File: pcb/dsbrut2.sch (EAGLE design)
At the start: 11 parts, among them IC1 4175D, IC2 74HC125D, IC3 MEGA8-AI

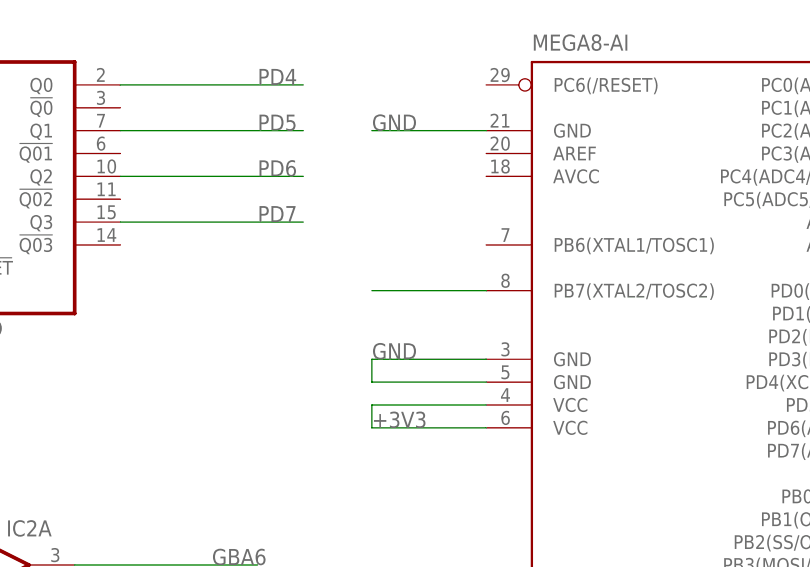
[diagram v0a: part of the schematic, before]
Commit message: updated isp progheader - please verify orientation
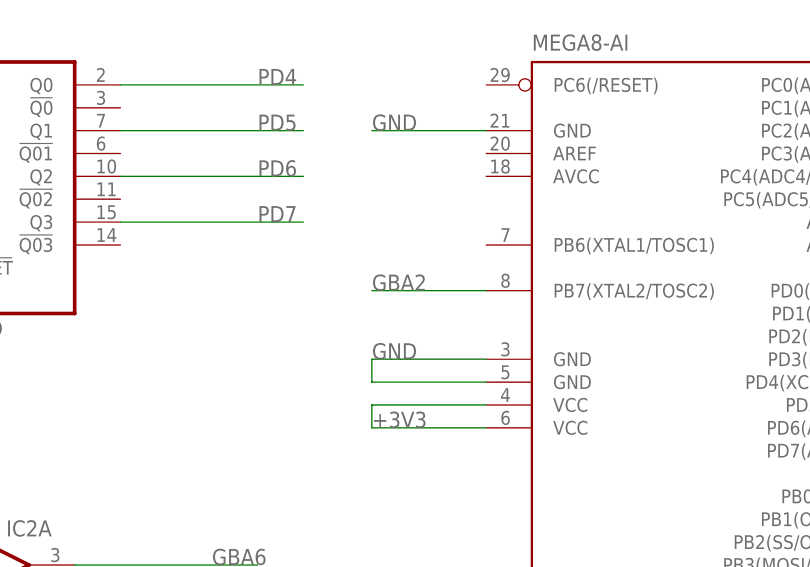
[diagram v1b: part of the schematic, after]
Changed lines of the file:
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@@
 <layer number="122" name="_bsilk" color="7" fill="1" visible="yes" active="yes"/>
 <layer number="125" name="_tNames" color="7" fill="1" visible="yes" active="yes"/>
+<layer number="131" name="prix" color="7" fill="1" visible="yes" active="yes"/>
+<layer number="132" name="test" color="7" fill="1" visible="yes" active="yes"/>
 <layer number="144" name="Drill_legend" color="7" fill="1" visible="yes" active="yes"/>
 <layer number="151" name="HeatSink" color="7" fill="1" visible="yes" active="yes"/>
@@
 <pinref part="IC3" gate="G$1" pin="PB7(XTAL2/TOSC2)"/>
 <wire x1="109.22" y1="127" x2="96.52" y2="127" width="0.1524" layer="91"/>
-</segment>
-<segment>
+<label x="96.52" y="127" size="1.778" layer="95"/>
+</segment>
+<segment>

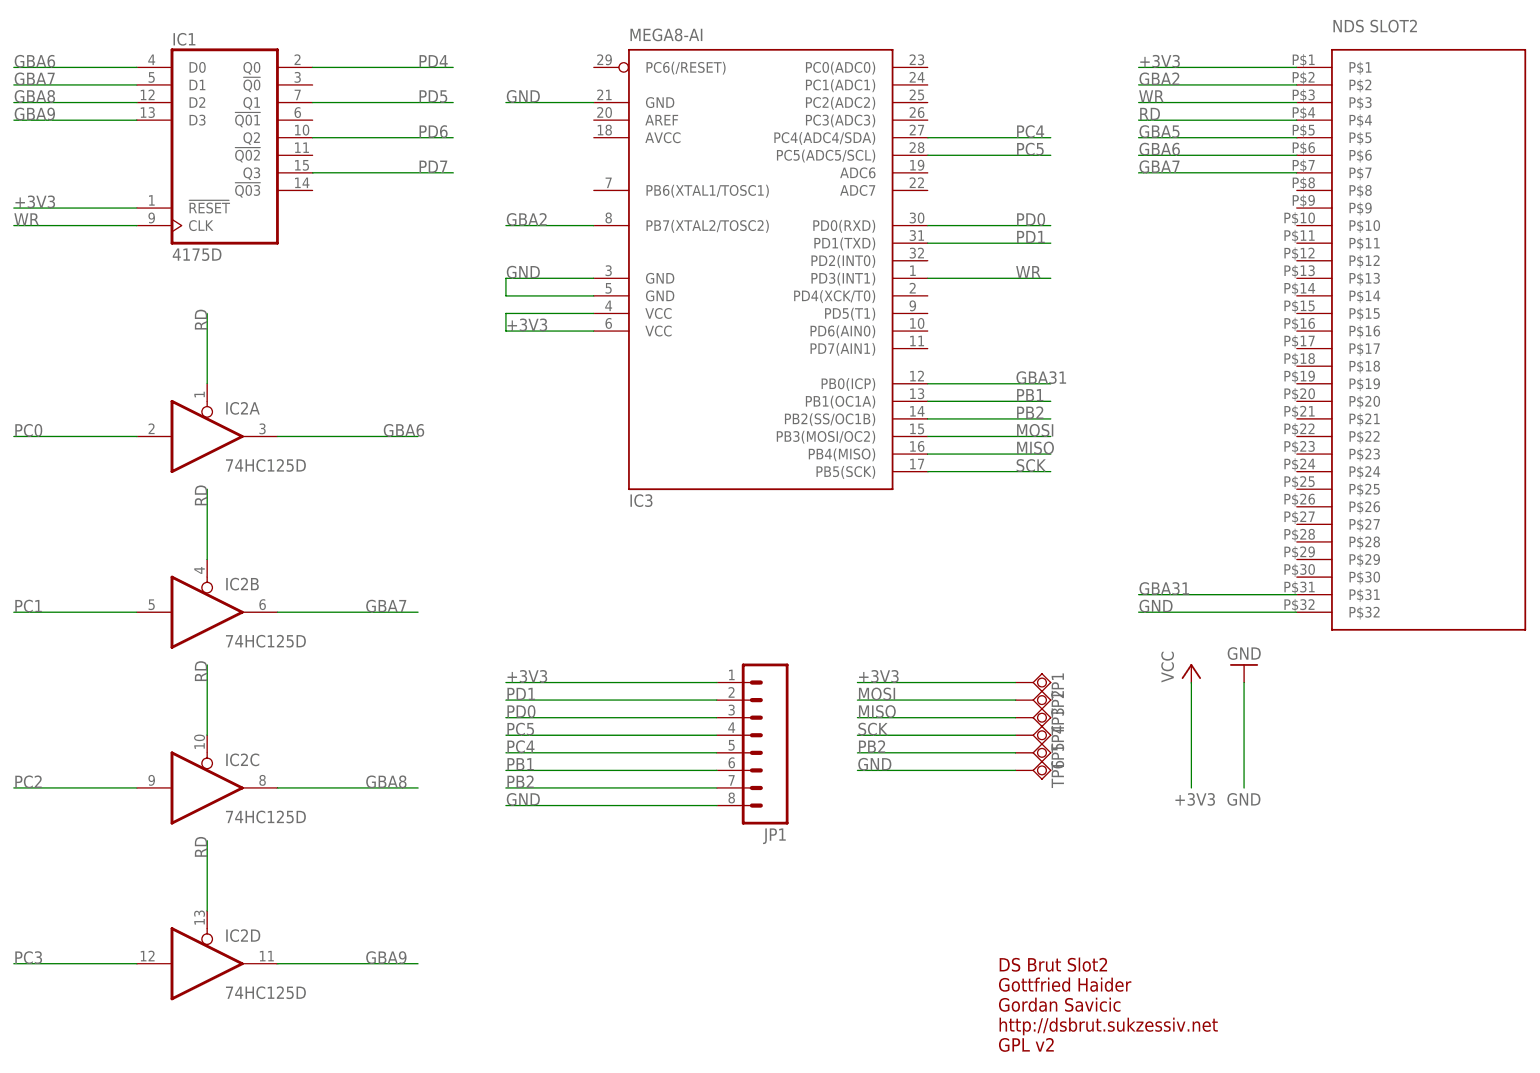
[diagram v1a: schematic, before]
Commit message: added rst, sck led, aref vcc, cleanup
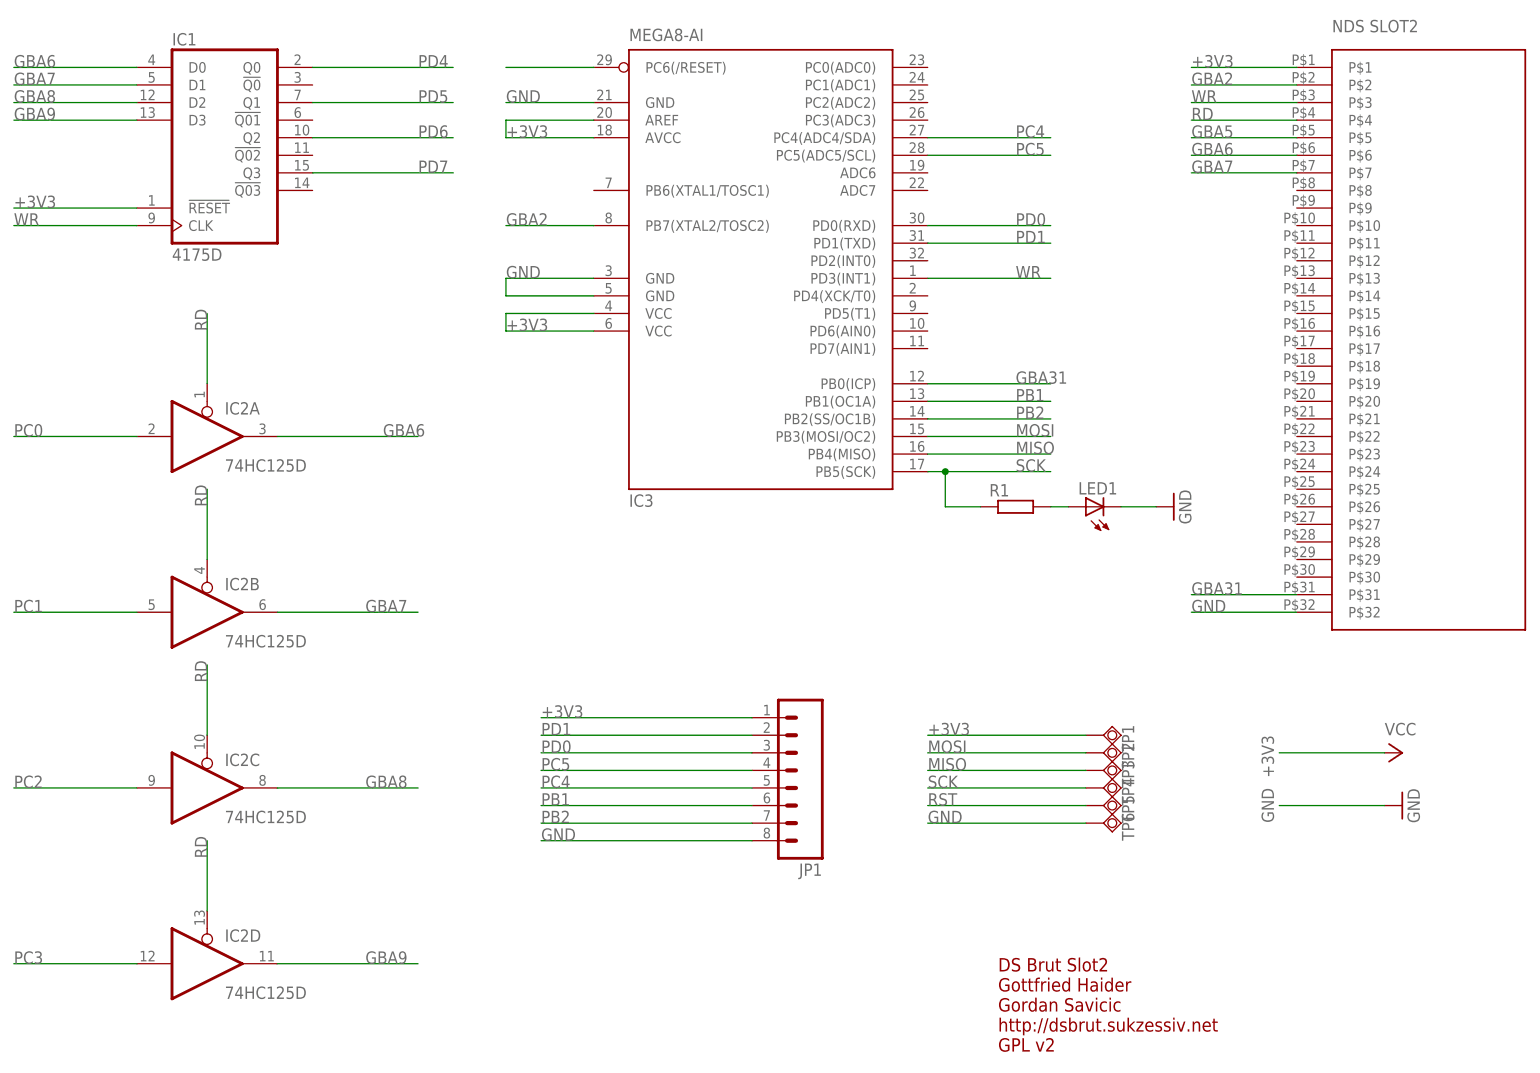
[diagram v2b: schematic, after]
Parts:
- added LED1: (no value), SparkFunEagle-6-6-07:LED0603
- added R1: (no value), rcl:R-EU_M0805
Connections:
- new net N$4: LED1.A, R1.2
- new net RST: IC3.PC6(/RESET), TP5.TP
- net +3V3: now also IC3.AREF, IC3.AVCC
- net GND: now also LED1.C
- net PB2: no longer TP5.TP
- net SCK: now also R1.1
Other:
- moved on the sheet: JP1, TP1, TP2, TP3, TP4, TP5, TP6

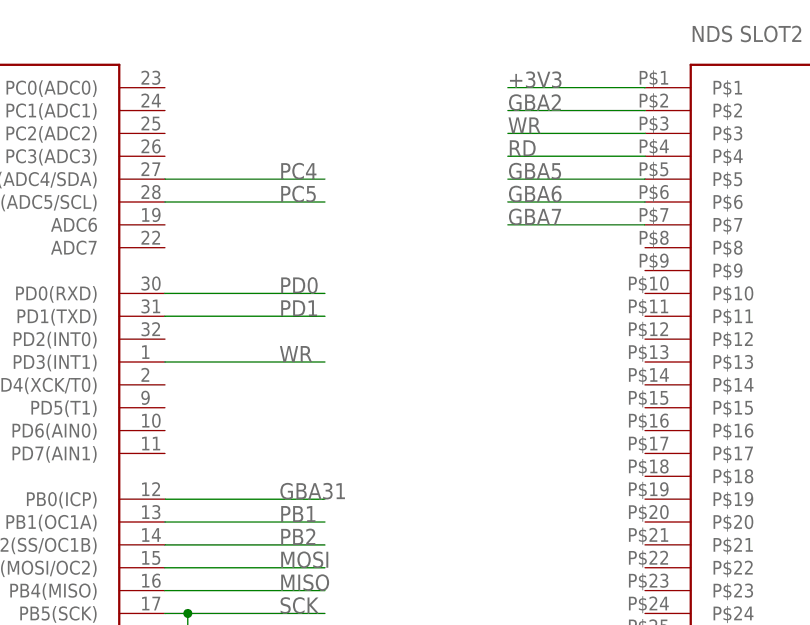
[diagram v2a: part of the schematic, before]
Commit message: Add GBA{8,9} and connections between IC{1,2} and the AtMega
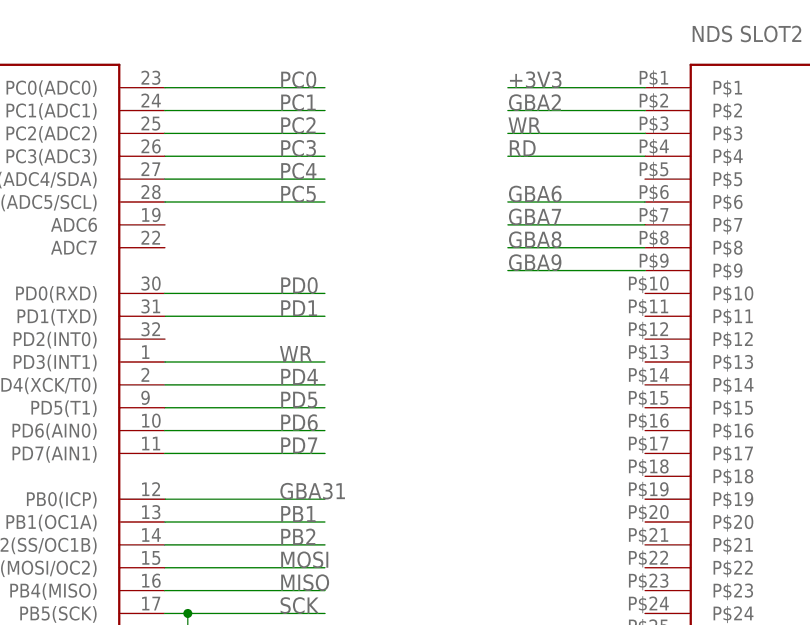
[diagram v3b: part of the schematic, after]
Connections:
- removed net GBA5: U$1.P$5
- net GBA8: now also U$1.P$8
- net GBA9: now also U$1.P$9
- net PC0: now also IC3.PC0(ADC0)
- net PC1: now also IC3.PC1(ADC1)
- net PC2: now also IC3.PC2(ADC2)
- net PC3: now also IC3.PC3(ADC3)
- net PD4: now also IC3.PD4(XCK/T0)
- net PD5: now also IC3.PD5(T1)
- net PD6: now also IC3.PD6(AIN0)
- net PD7: now also IC3.PD7(AIN1)
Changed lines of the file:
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@@
 <label x="83.82" y="149.86" size="1.778" layer="95"/>
+</segment>
+<segment>
+<pinref part="IC3" gate="G$1" pin="PD4(XCK/T0)"/>
+<wire x1="157.48" y1="116.84" x2="175.26" y2="116.84" width="0.1524" layer="91"/>
+<label x="170.18" y="116.84" size="1.778" layer="95"/>
 </segment>
 </net>
@@
 <label x="83.82" y="144.78" size="1.778" layer="95"/>
 </segment>
+<segment>
+<pinref part="IC3" gate="G$1" pin="PD5(T1)"/>
+<wire x1="157.48" y1="114.3" x2="175.26" y2="114.3" width="0.1524" layer="91"/>
+<label x="170.18" y="114.3" size="1.778" layer="95"/>
+</segment>
 </net>
 <net name="WR" class="0">
@@
 <label x="83.82" y="139.7" size="1.778" layer="95"/>
 </segment>
+<segment>
+<pinref part="IC3" gate="G$1" pin="PD6(AIN0)"/>
+<wire x1="157.48" y1="111.76" x2="175.26" y2="111.76" width="0.1524" layer="91"/>
+<label x="170.18" y="111.76" size="1.778" layer="95"/>
+</segment>
 </net>
 <net name="GBA8" class="0">
@@
 <label x="76.2" y="45.72" size="1.778" layer="95"/>
 </segment>
+<segment>
+<pinref part="U$1" gate="G$1" pin="P$8"/>
+<wire x1="210.82" y1="132.08" x2="195.58" y2="132.08" width="0.1524" layer="91"/>
+<label x="195.58" y="132.08" size="1.778" layer="95"/>
+</segment>
 </net>
 <net name="GBA9" class="0">
@@
 <label x="76.2" y="20.32" size="1.778" layer="95"/>
 </segment>
+<segment>
+<pinref part="U$1" gate="G$1" pin="P$9"/>
+<wire x1="210.82" y1="129.54" x2="195.58" y2="129.54" width="0.1524" layer="91"/>
+<label x="195.58" y="129.54" size="1.778" layer="95"/>
+</segment>
 </net>
 <net name="PD7" class="0">
@@
 <label x="83.82" y="134.62" size="1.778" layer="95"/>
 </segment>
+<segment>
+<pinref part="IC3" gate="G$1" pin="PD7(AIN1)"/>
+<wire x1="157.48" y1="109.22" x2="175.26" y2="109.22" width="0.1524" layer="91"/>
+<label x="170.18" y="109.22" size="1.778" layer="95"/>
+</segment>
 </net>
 <net name="PC3" class="0">
@@
 <label x="25.4" y="20.32" size="1.778" layer="95"/>
 </segment>
+<segment>
+<pinref part="IC3" gate="G$1" pin="PC3(ADC3)"/>
+<wire x1="157.48" y1="142.24" x2="175.26" y2="142.24" width="0.1524" layer="91"/>
+<label x="170.18" y="142.24" size="1.778" layer="95"/>
+</segment>
 </net>
 <net name="PC1" class="0">
@@
 <label x="25.4" y="71.12" size="1.778" layer="95"/>
 </segment>
+<segment>
+<pinref part="IC3" gate="G$1" pin="PC1(ADC1)"/>
+<wire x1="157.48" y1="147.32" x2="175.26" y2="147.32" width="0.1524" layer="91"/>
+<label x="170.18" y="147.32" size="1.778" layer="95"/>
+</segment>
 </net>
 <net name="PC0" class="0">
@@
 <label x="25.4" y="96.52" size="1.778" layer="95"/>
 </segment>
+<segment>
+<pinref part="IC3" gate="G$1" pin="PC0(ADC0)"/>
+<wire x1="157.48" y1="149.86" x2="175.26" y2="149.86" width="0.1524" layer="91"/>
+<label x="170.18" y="149.86" size="1.778" layer="95"/>
+</segment>
 </net>
 <net name="RD" class="0">
@@
 <label x="25.4" y="45.72" size="1.778" layer="95"/>
 </segment>
+<segment>
+<pinref part="IC3" gate="G$1" pin="PC2(ADC2)"/>
+<wire x1="157.48" y1="144.78" x2="175.26" y2="144.78" width="0.1524" layer="91"/>
+<label x="170.18" y="144.78" size="1.778" layer="95"/>
+</segment>
 </net>
 <net name="GBA31" class="0">
@@
 </segment>
 </net>
-<net name="GBA5" class="0">
-<segment>
-<pinref part="U$1" gate="G$1" pin="P$5"/>
-<wire x1="210.82" y1="139.7" x2="195.58" y2="139.7" width="0.1524" layer="91"/>
-<label x="195.58" y="139.7" size="1.778" layer="95"/>
-</segment>
-</net>

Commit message: Connected RD to ATmega, added TX/RX labels, removed ground plane underneath Slot -2 pins
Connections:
- net RD: now also IC3.PD2(INT0)
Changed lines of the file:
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@@
 <label x="195.58" y="142.24" size="1.778" layer="95"/>
+</segment>
+<segment>
+<pinref part="IC3" gate="G$1" pin="PD2(INT0)"/>
+<wire x1="157.48" y1="121.92" x2="175.26" y2="121.92" width="0.1524" layer="91"/>
+<label x="170.18" y="121.92" size="1.778" layer="95"/>
 </segment>
 </net>

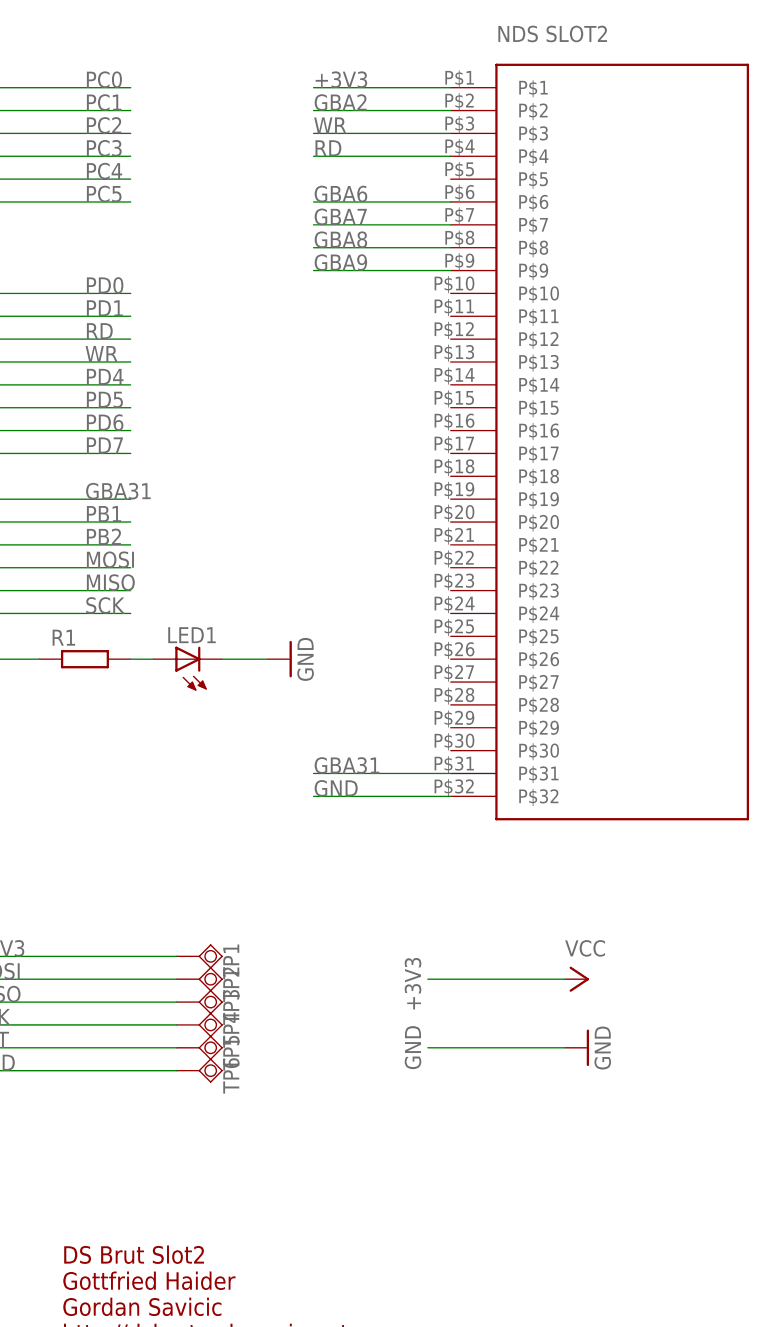
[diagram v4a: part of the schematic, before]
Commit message: added fuse, fixed ic1 power supply with VSS
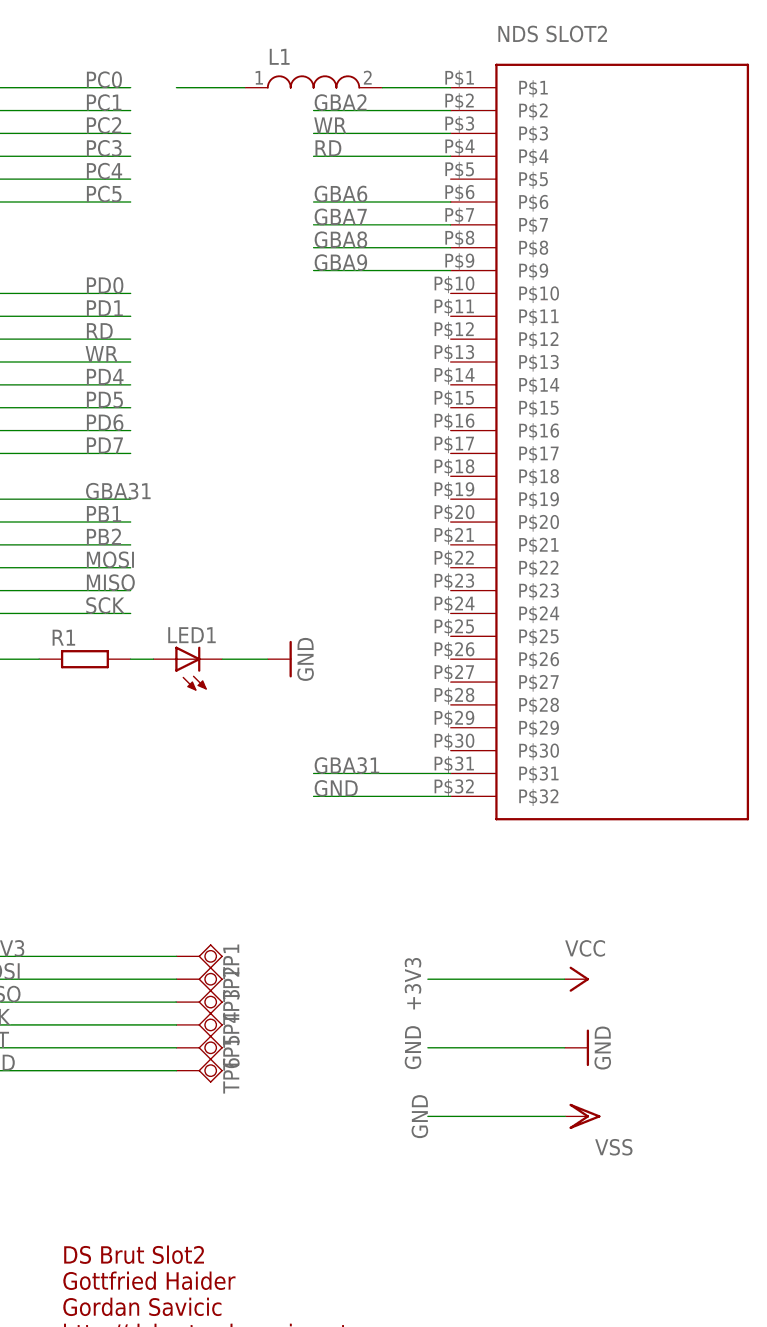
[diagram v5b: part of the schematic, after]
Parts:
- added L1: INDUCTOR-L1812, dp_devices:INDUCTOR-L1812
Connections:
- new net N$1: L1.2, U$1.P$1
- net +3V3: now also L1.1; no longer U$1.P$1
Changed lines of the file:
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@@
 <part name="GND3" library="supply1" deviceset="GND" device=""/>
 <part name="R1" library="rcl" deviceset="R-EU_" device="M0805"/>
+<part name="VSS1" library="supply1" deviceset="VSS" device=""/>
+<part name="L1" library="dp_devices" deviceset="INDUCTOR" device="-L1812"/>
 </parts>
 <sheets>
@@
 <instance part="GND3" gate="1" x="193.04" y="86.36" rot="R90"/>
 <instance part="R1" gate="G$1" x="170.18" y="86.36"/>
+<instance part="VSS1" gate="G$1" x="226.06" y="35.56" rot="R90"/>
+<instance part="L1" gate="L" x="195.58" y="149.86" smashed="yes">
+<attribute name="NAME" x="190.5" y="152.4" size="1.778" layer="95"/>
+</instance>
 </instances>
 <busses>
@@
 <wire x1="43.18" y1="129.54" x2="25.4" y2="129.54" width="0.1524" layer="91"/>
 <label x="25.4" y="129.54" size="1.778" layer="95"/>
-</segment>
-<segment>
-<pinref part="U$1" gate="G$1" pin="P$1"/>
-<wire x1="210.82" y1="149.86" x2="195.58" y2="149.86" width="0.1524" layer="91"/>
-<label x="195.58" y="149.86" size="1.778" layer="95"/>
 </segment>
 <segment>
@@
 <label x="96.52" y="139.7" size="1.778" layer="95"/>
 </segment>
+<segment>
+<pinref part="L1" gate="L" pin="1"/>
+<wire x1="187.96" y1="149.86" x2="180.34" y2="149.86" width="0.1524" layer="91"/>
+</segment>
 </net>
 <net name="PD1" class="0">
@@
 <pinref part="LED1" gate="G$1" pin="C"/>
 <pinref part="GND3" gate="1" pin="GND"/>
+</segment>
+<segment>
+<wire x1="208.28" y1="35.56" x2="223.52" y2="35.56" width="0.1524" layer="91"/>
+<label x="208.28" y="33.02" size="1.778" layer="95" rot="R90"/>
+<pinref part="VSS1" gate="G$1" pin="VSS"/>
 </segment>
 </net>
@@
 </segment>
 </net>
+<net name="N$1" class="0">
+<segment>
+<pinref part="U$1" gate="G$1" pin="P$1"/>
+<pinref part="L1" gate="L" pin="2"/>
+<wire x1="210.82" y1="149.86" x2="203.2" y2="149.86" width="0.1524" layer="91"/>
+</segment>
+</net>
